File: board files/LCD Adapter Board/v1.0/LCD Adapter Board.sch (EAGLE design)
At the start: 3 parts

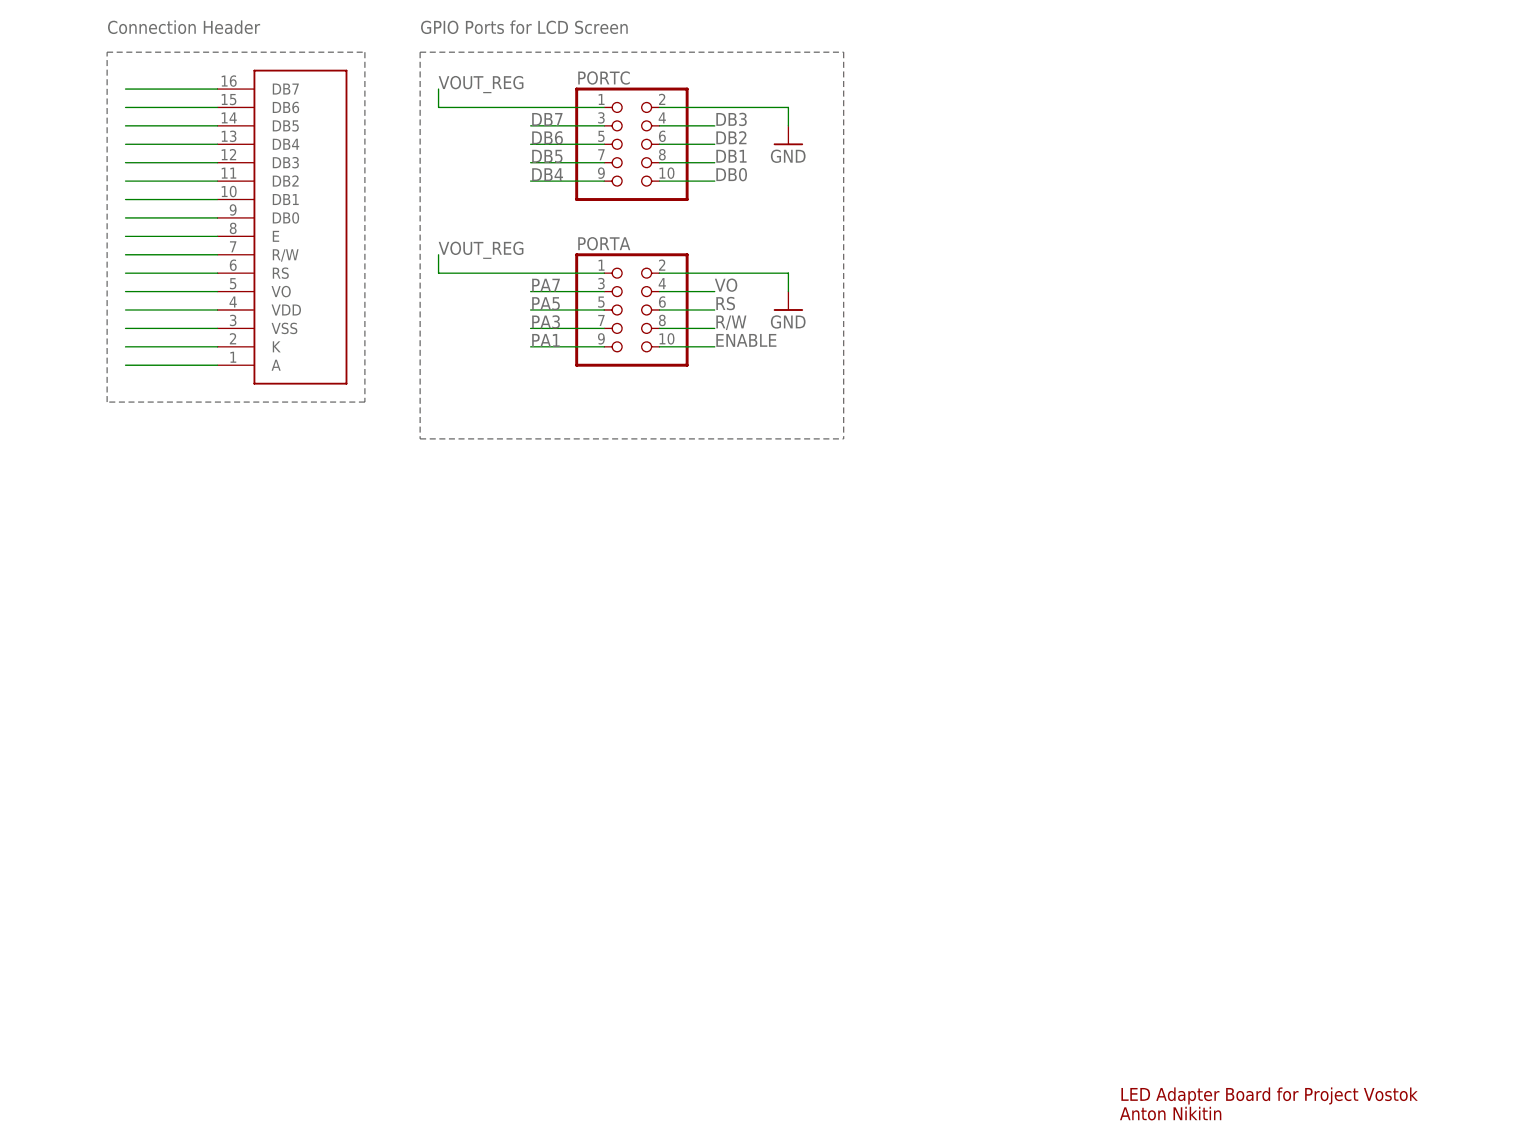
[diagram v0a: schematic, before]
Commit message: add boost converter
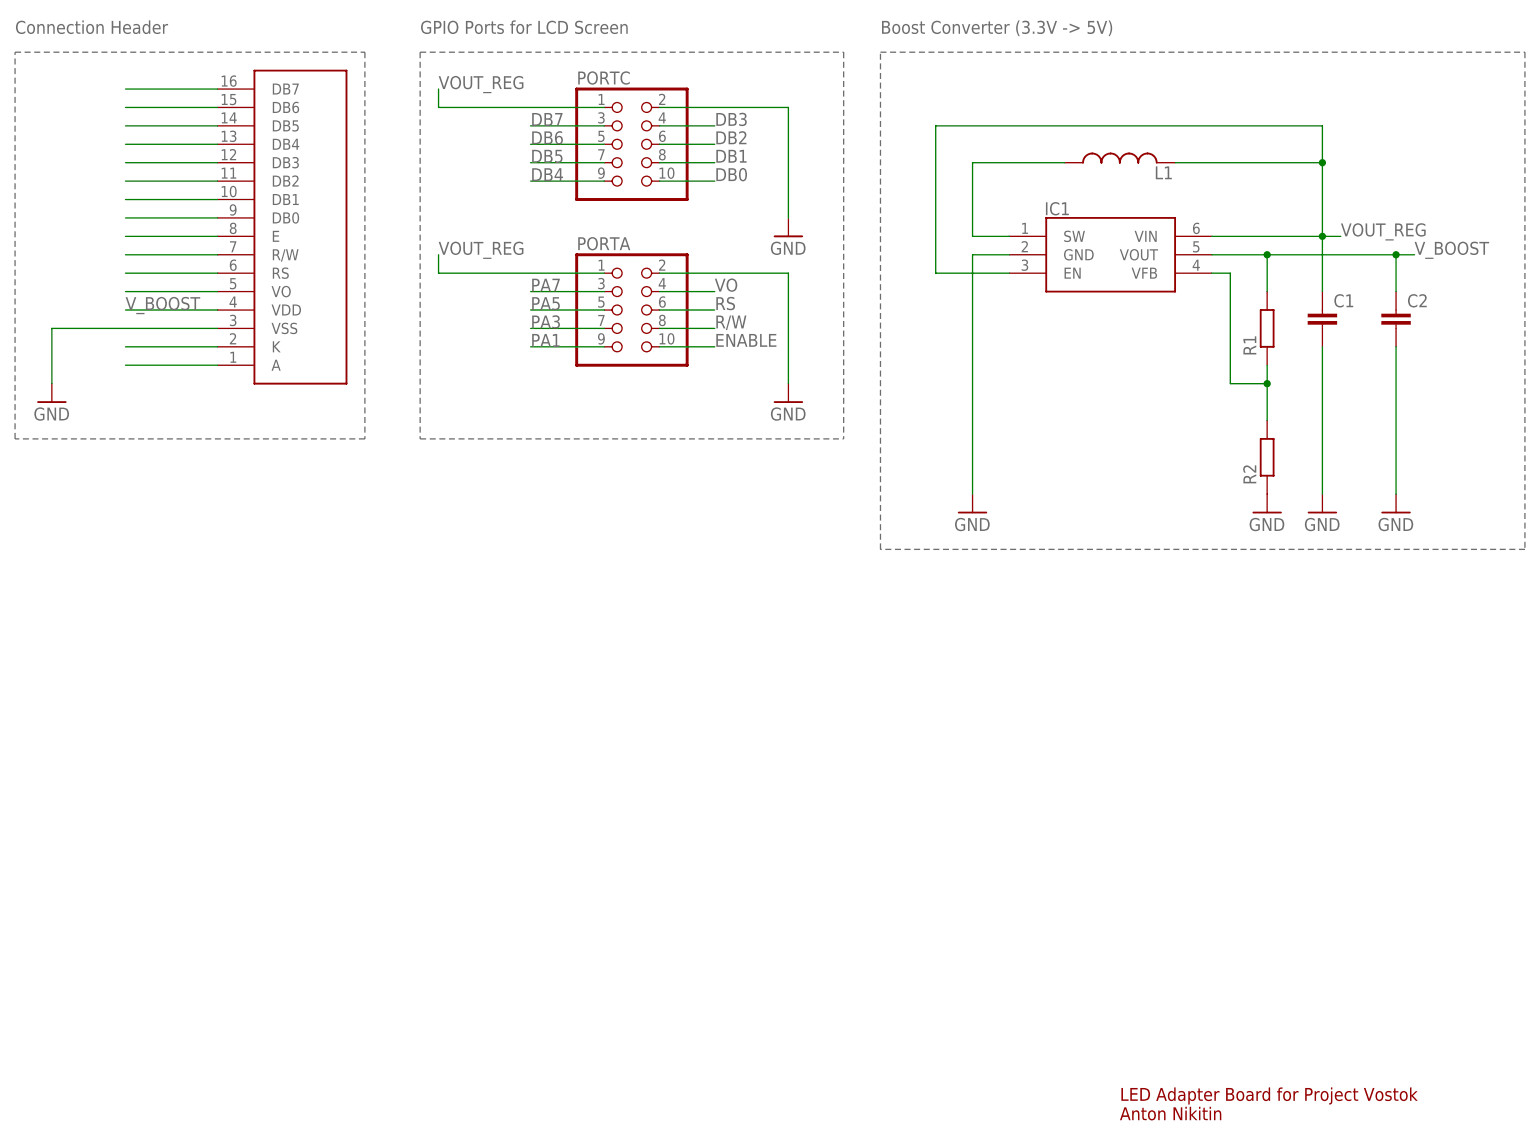
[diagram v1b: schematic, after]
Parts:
- added C1, C2: (no value), rcl:C-EUC0603
- added IC1: MCP1640BT-I_CHY, SamacSys_Parts:MCP1640BT-I_CHY
- added L1: (no value), rcl:L-USL0201
- added R1, R2: (no value), rcl:R-EU_R0603
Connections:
- removed net N$3: DS1.VSS
- removed net N$4: DS1.VDD
- new net N$17: IC1.SW, L1.1
- new net N$19: IC1.VFB, R1.1, R2.2
- new net V_BOOST: C2.1, DS1.VDD, IC1.VOUT, R1.2
- net GND: now also C1.2, C2.2, DS1.VSS, IC1.GND, R2.1
- net VOUT_REG: now also C1.1, IC1.EN, IC1.VIN, L1.2
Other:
- note added: "Boost Converter (3.3V -> 5V)"
